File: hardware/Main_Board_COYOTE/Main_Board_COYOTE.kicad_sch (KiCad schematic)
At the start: 31 parts, among them J2 Conn_01x05_Pin, J3 Conn_01x05_Pin, J3 FTDI, J4 V+-, Q1 2N7002, SW1 SW_SPST, SW2 START, SW3 START, U2 AMS1117-3.3, U2 ESP32-WROOM-32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

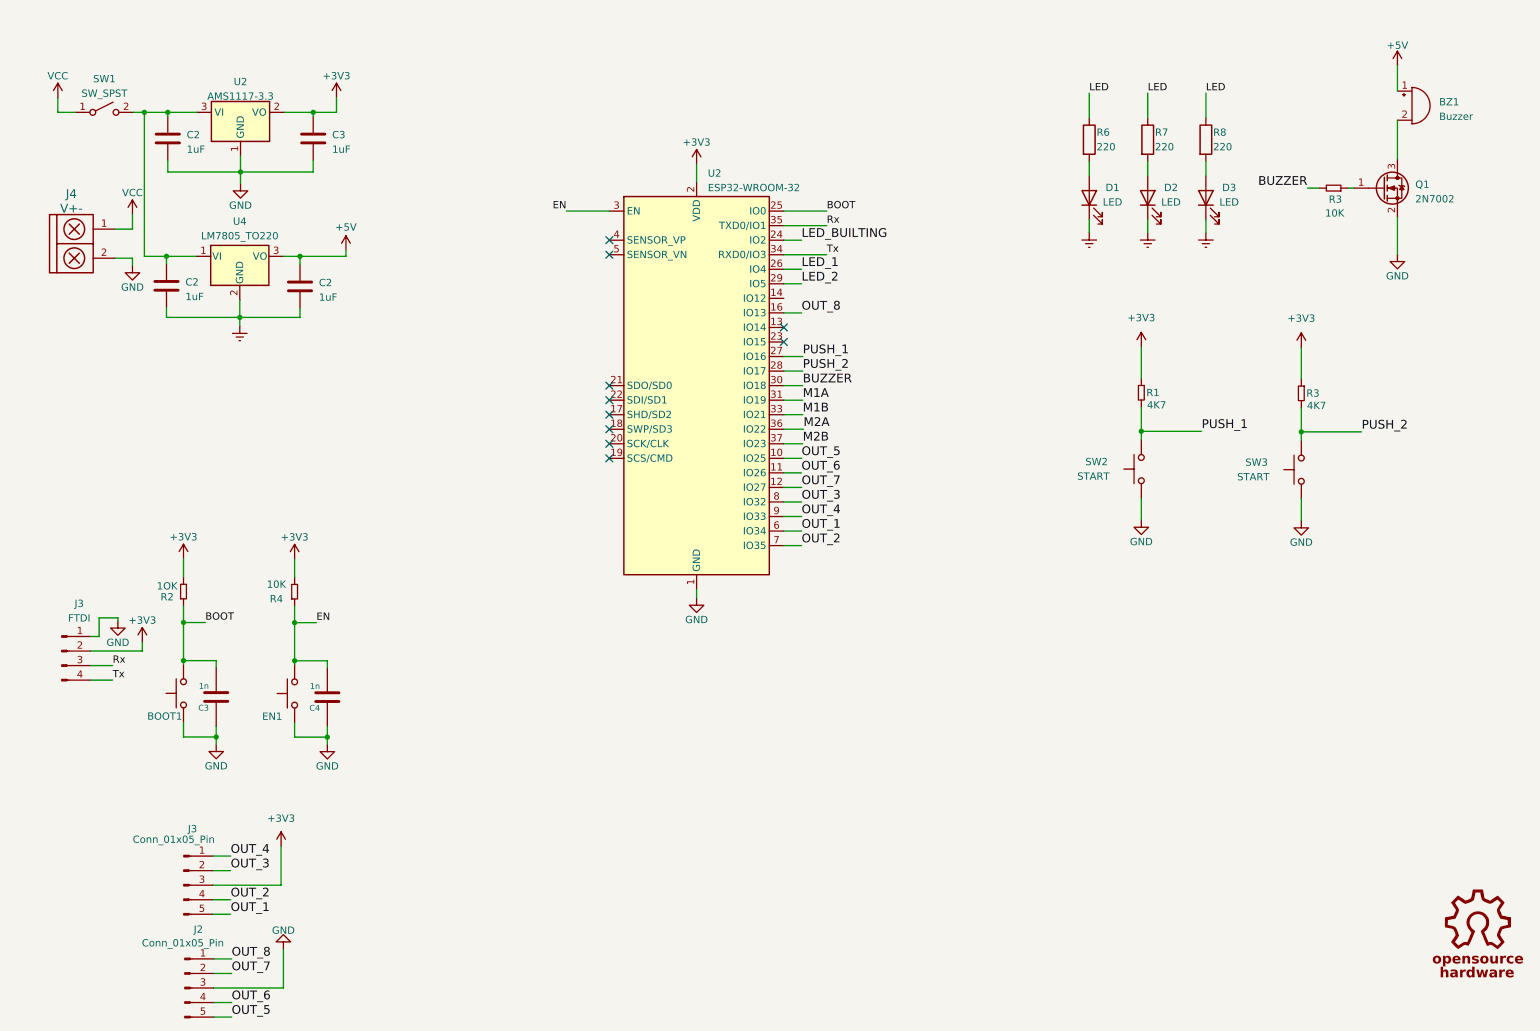
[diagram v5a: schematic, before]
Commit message: SCH del velocista terminado
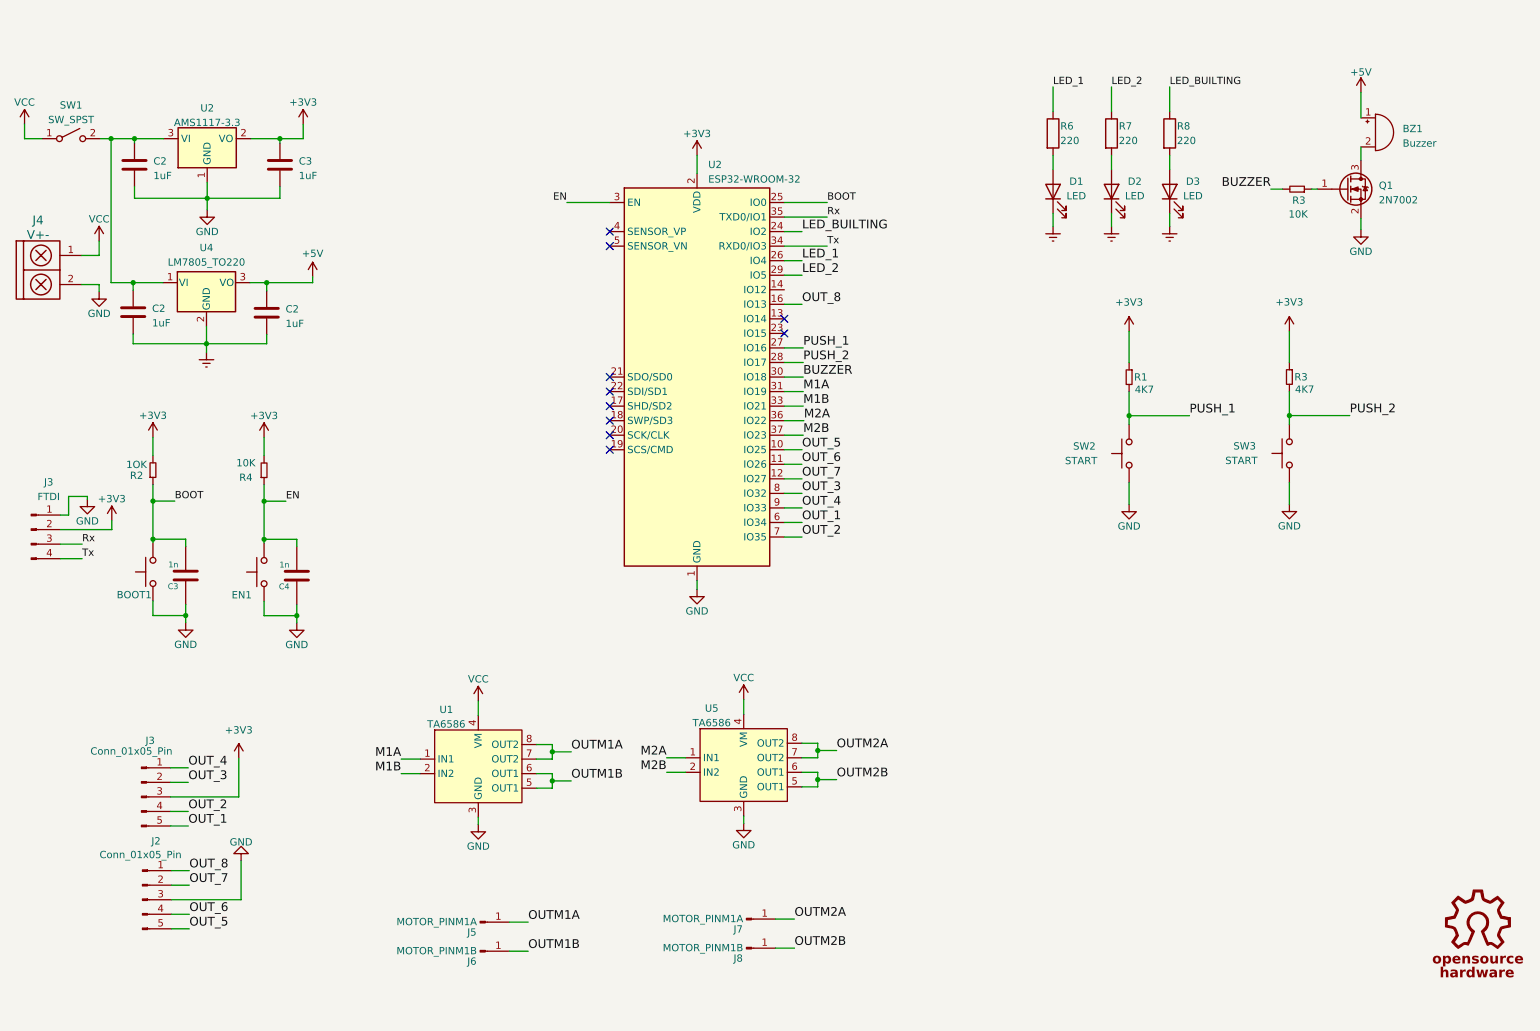
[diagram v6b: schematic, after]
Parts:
- added J5, J7: MOTOR_PINM1A, Connector:Banana_Jack_1Pin, symbol Connector:Conn_01x01_Pin
- added J6, J8: MOTOR_PINM1B, Connector:Banana_Jack_1Pin, symbol Connector:Conn_01x01_Pin
- added U1, U5: TA6586, Package_DIP:DIP-8_W7.62mm, symbol EESTN5-v2:TA6586
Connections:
- net GND: now also U1.3 (GND), U5.3 (GND)
- net LED_1: now also R6.1
- net LED_2: now also R7.1
- net LED_BUILTING: now also R8.1
- net M1A: now also U1.1 (IN1)
- net M1B: now also U1.2 (IN2)
- net M2A: now also U5.1 (IN1)
- net M2B: now also U5.2 (IN2)
- net VCC: now also U1.4 (VM), U5.4 (VM)
- removed net LED: R6.1, R7.1, R8.1
- new net OUTM1A: J5.1 (Pin_1), U1.7 (OUT2), U1.8 (OUT2)
- new net OUTM1B: J6.1 (Pin_1), U1.5 (OUT1), U1.6 (OUT1)
- new net OUTM2A: J7.1 (Pin_1), U5.7 (OUT2), U5.8 (OUT2)
- new net OUTM2B: J8.1 (Pin_1), U5.5 (OUT1), U5.6 (OUT1)
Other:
- moved on the sheet: BOOT1, BZ1, C2, C3, C4, D1, D2, D3, EN1, J2, J3, J4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
